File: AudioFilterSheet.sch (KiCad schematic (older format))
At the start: 16 parts, among them P1 R, P2 R, P3 R, P4 R, P5 R, P6 R

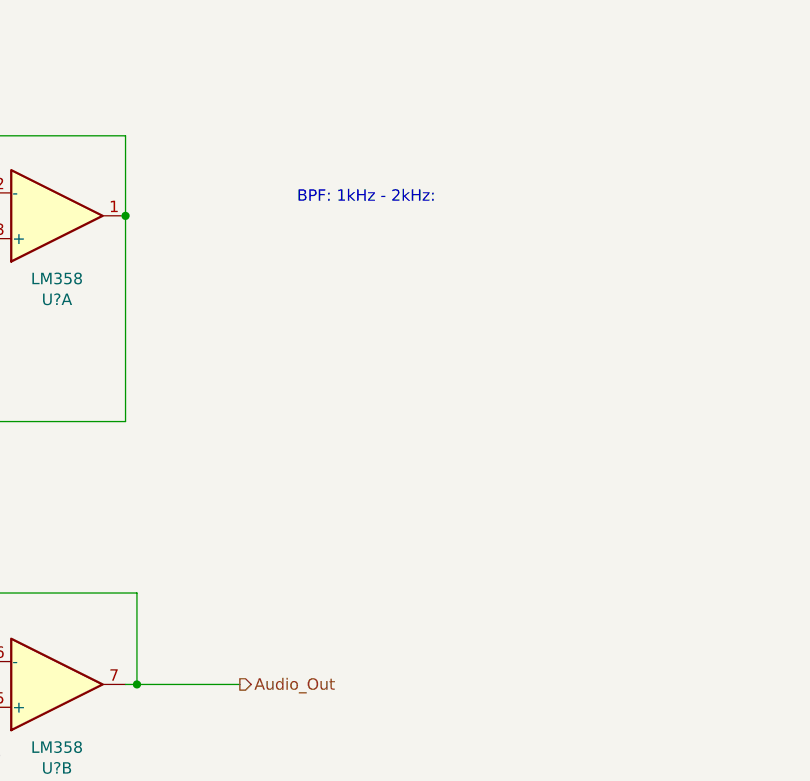
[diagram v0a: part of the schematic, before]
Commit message: Filter calculations, gain stage, oscillation protection
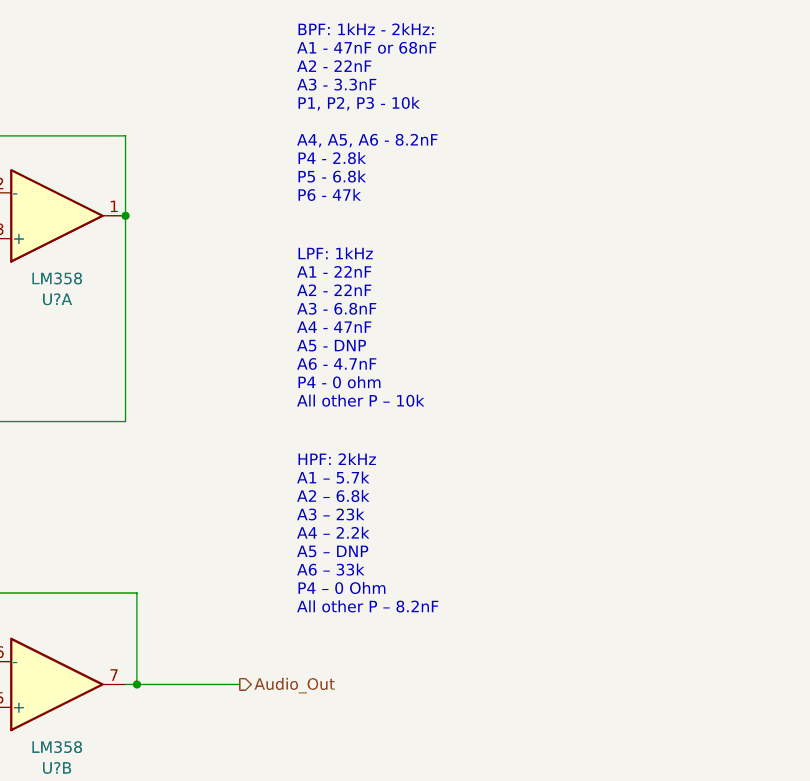
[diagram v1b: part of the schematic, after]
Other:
- note added: "BPF: 1kHz - 2kHz:\nA1 - 47nF or 68nF\nA2 - 22nF\nA3 - 3.3nF\nP1, P2, P3 - 10k\n\nA4, A5, A6 - 8.2nF\nP4 - 2.8k\nP5 - 6.8k\nP6 - 47k"
- note added: "HPF: 2kHz \nA1 – 5.7k \nA2 – 6.8k \nA3 – 23k \nA4 – 2.2k \nA5 – DNP \nA6 – 33k \nP4 – 0 Ohm \nAll other P – 8.2nF"
- note added: "LPF: 1kHz \nA1 - 22nF \nA2 - 22nF \nA3 - 6.8nF \nA4 - 47nF \nA5 - DNP \nA6 - 4.7nF \nP4 - 0 ohm \nAll other P – 10k"
- note removed: "BPF: 1kHz - 2kHz:"
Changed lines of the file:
@@
 	4450 3150 3950 3150
 Text Notes 5800 1450 0    50   ~ 0
-BPF: 1kHz - 2kHz:
+BPF: 1kHz - 2kHz:\nA1 - 47nF or 68nF\nA2 - 22nF\nA3 - 3.3nF\nP1, P2, P3 - 10k\n\nA4, A5, A6 - 8.2nF\nP4 - 2.8k\nP5 - 6.8k\nP6 - 47k
 $Comp
 L Device:C C?
@@
 	8850 2450 8350 2450
 Connection ~ 8350 2450
+Text Notes 5800 2350 0    50   ~ 0
+LPF: 1kHz \nA1 - 22nF \nA2 - 22nF \nA3 - 6.8nF \nA4 - 47nF \nA5 - DNP \nA6 - 4.7nF \nP4 - 0 ohm \nAll other P – 10k
+Text Notes 5800 3250 0    50   ~ 0
+HPF: 2kHz \nA1 – 5.7k \nA2 – 6.8k \nA3 – 23k \nA4 – 2.2k \nA5 – DNP \nA6 – 33k \nP4 – 0 Ohm \nAll other P – 8.2nF
 $EndSCHEMATC

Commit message: WIP
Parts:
- U? (x3): value LM358 -> OPA1678; symbol Amplifier_Operational:LM358 -> Amplifier_Operational:OPA1678
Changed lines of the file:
@@
 $EndComp
 $Comp
-L Amplifier_Operational:LM358 U?
+L Amplifier_Operational:OPA1678 U?
 U 3 1 5E3A2220
 P 8450 2150
@@
 AR Path="/5E41292B/5E39A609/5E3A2220" Ref="U?"  Part="3"
 F 0 "U?" H 8408 2196 50  0000 L CNN
-F 1 "LM358" H 8408 2105 50  0000 L CNN
+F 1 "OPA1678" H 8408 2105 50  0000 L CNN
 F 2 "" H 8450 2150 50  0001 C CNN
 F 3 "http://www.ti.com/lit/ds/symlink/lm2904-n.pdf" H 8450 2150 50  0001 C CNN
@@
 $EndComp
 $Comp
-L Amplifier_Operational:LM358 U?
+L Amplifier_Operational:OPA1678 U?
 U 1 1 5E3A55EC
 P 4750 1500
@@
 AR Path="/5E41292B/5E39A609/5E3A55EC" Ref="U?"  Part="1"
 F 0 "U?" H 4750 1867 50  0000 C CNN
-F 1 "LM358" H 4750 1776 50  0000 C CNN
+F 1 "OPA1678" H 4750 1776 50  0000 C CNN
 F 2 "" H 4750 1500 50  0001 C CNN
 F 3 "http://www.ti.com/lit/ds/symlink/lm2904-n.pdf" H 4750 1500 50  0001 C CNN
@@
 $EndComp
 $Comp
-L Amplifier_Operational:LM358 U?
+L Amplifier_Operational:OPA1678 U?
 U 2 1 5E3A6C1B
 P 4750 3550
@@
 AR Path="/5E41292B/5E39A609/5E3A6C1B" Ref="U?"  Part="2"
 F 0 "U?" H 4750 3917 50  0000 C CNN
-F 1 "LM358" H 4750 3826 50  0000 C CNN
+F 1 "OPA1678" H 4750 3826 50  0000 C CNN
 F 2 "" H 4750 3550 50  0001 C CNN
 F 3 "http://www.ti.com/lit/ds/symlink/lm2904-n.pdf" H 4750 3550 50  0001 C CNN

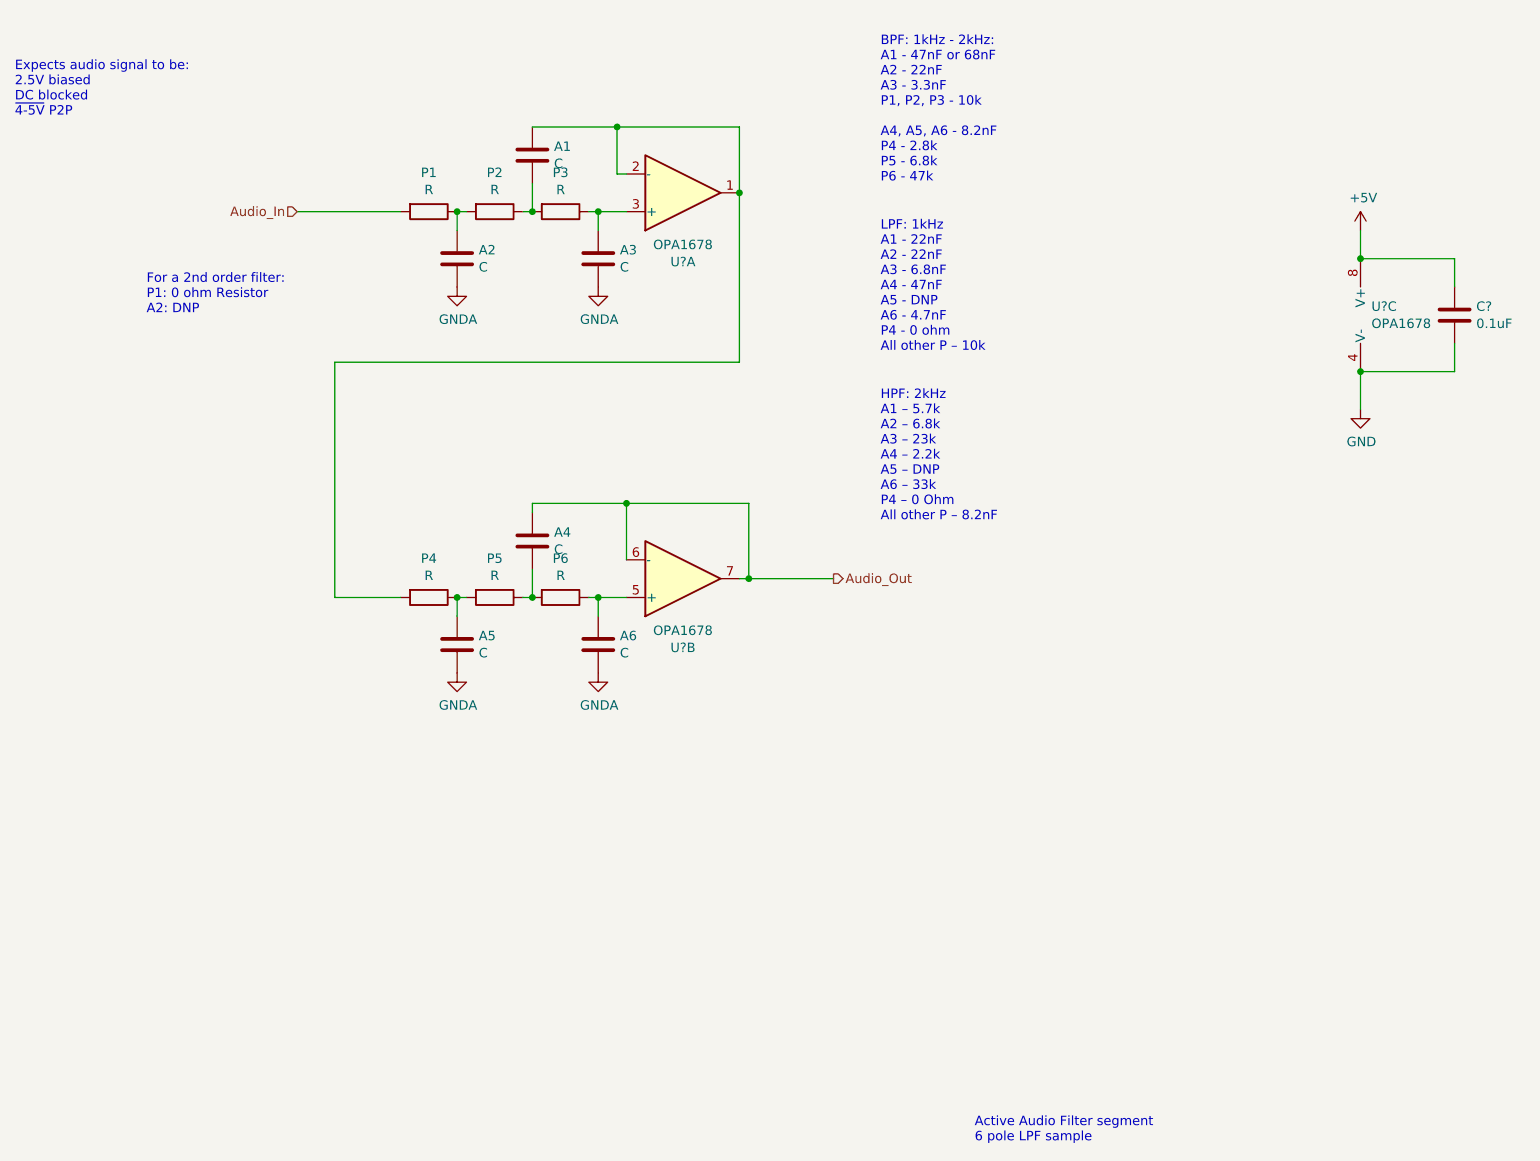
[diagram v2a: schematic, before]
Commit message: Ferrite beads and annotations
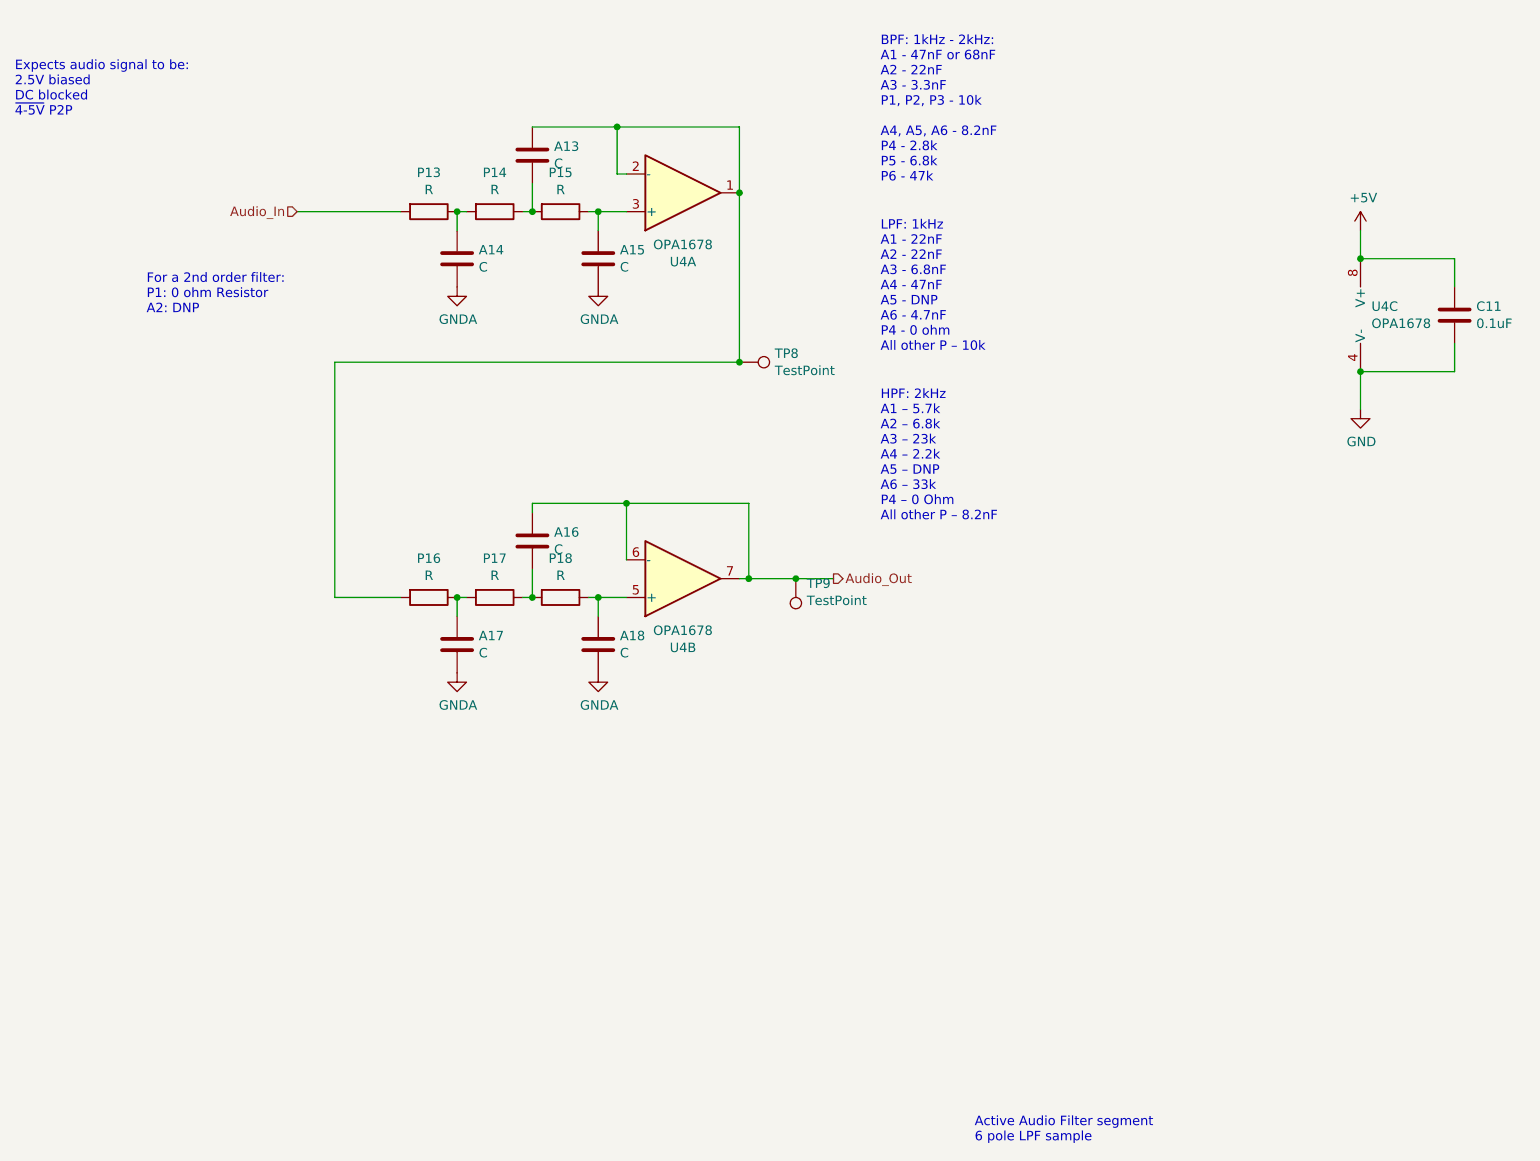
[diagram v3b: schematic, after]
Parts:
- added TP2, TP3: TestPoint, symbol Connector:TestPoint
- gave numbers to parts that had none: 2
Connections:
- net Audio_Out: now also TP3.1
- net at A1.1, P4.2, U1.1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: now also TP2.1

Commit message: Layout, 2020-05 order
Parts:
- removed TP2, TP3: TestPoint, symbol Connector:TestPoint
- A1, A2, A3, A4, A5, A6, C3, P1, P2, P3, P4, P5, P6: footprint (none) -> Capacitors_SMD:C_0805_HandSoldering
- U1: footprint (none) -> SMD_Packages:SOIC-8-N
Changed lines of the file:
@@
 AR Path="/5E41281A/5E39A609/5E39FBC3" Ref="P7"  Part="1"
 AR Path="/5E41292B/5E39A609/5E39FBC3" Ref="P13"  Part="1"
-F 0 "P13" V 3193 1600 50  0000 C CNN
+F 0 "P1" V 3193 1600 50  0000 C CNN
 F 1 "R" V 3284 1600 50  0000 C CNN
-F 2 "" V 3330 1600 50  0001 C CNN
+F 2 "Capacitors_SMD:C_0805_HandSoldering" V 3330 1600 50  0001 C CNN
 F 3 "~" H 3400 1600 50  0001 C CNN
 	1    3400 1600
@@
 AR Path="/5E41281A/5E39A609/5E39FFC0" Ref="P8"  Part="1"
 AR Path="/5E41292B/5E39A609/5E39FFC0" Ref="P14"  Part="1"
-F 0 "P14" V 3543 1600 50  0000 C CNN
+F 0 "P2" V 3543 1600 50  0000 C CNN
 F 1 "R" V 3634 1600 50  0000 C CNN
-F 2 "" V 3680 1600 50  0001 C CNN
+F 2 "Capacitors_SMD:C_0805_HandSoldering" V 3680 1600 50  0001 C CNN
 F 3 "~" H 3750 1600 50  0001 C CNN
 	1    3750 1600
@@
 AR Path="/5E41281A/5E39A609/5E3A018A" Ref="P9"  Part="1"
 AR Path="/5E41292B/5E39A609/5E3A018A" Ref="P15"  Part="1"
-F 0 "P15" V 3893 1600 50  0000 C CNN
+F 0 "P3" V 3893 1600 50  0000 C CNN
 F 1 "R" V 3984 1600 50  0000 C CNN
-F 2 "" V 4030 1600 50  0001 C CNN
+F 2 "Capacitors_SMD:C_0805_HandSoldering" V 4030 1600 50  0001 C CNN
 F 3 "~" H 4100 1600 50  0001 C CNN
 	1    4100 1600
@@
 AR Path="/5E41281A/5E39A609/5E3A0389" Ref="A7"  Part="1"
 AR Path="/5E41292B/5E39A609/5E3A0389" Ref="A13"  Part="1"
-F 0 "A13" H 4065 1346 50  0000 L CNN
+F 0 "A1" H 4065 1346 50  0000 L CNN
 F 1 "C" H 4065 1255 50  0000 L CNN
-F 2 "" H 3988 1150 50  0001 C CNN
+F 2 "Capacitors_SMD:C_0805_HandSoldering" H 3988 1150 50  0001 C CNN
 F 3 "~" H 3950 1300 50  0001 C CNN
 	1    3950 1300
@@
 AR Path="/5E41281A/5E39A609/5E3A041B" Ref="A9"  Part="1"
 AR Path="/5E41292B/5E39A609/5E3A041B" Ref="A15"  Part="1"
-F 0 "A15" H 4415 1896 50  0000 L CNN
+F 0 "A3" H 4415 1896 50  0000 L CNN
 F 1 "C" H 4415 1805 50  0000 L CNN
-F 2 "" H 4338 1700 50  0001 C CNN
+F 2 "Capacitors_SMD:C_0805_HandSoldering" H 4338 1700 50  0001 C CNN
 F 3 "~" H 4300 1850 50  0001 C CNN
 	1    4300 1850
@@
 AR Path="/5E41281A/5E39A609/5E3A0747" Ref="A8"  Part="1"
 AR Path="/5E41292B/5E39A609/5E3A0747" Ref="A14"  Part="1"
-F 0 "A14" H 3665 1896 50  0000 L CNN
+F 0 "A2" H 3665 1896 50  0000 L CNN
 F 1 "C" H 3665 1805 50  0000 L CNN
-F 2 "" H 3588 1700 50  0001 C CNN
+F 2 "Capacitors_SMD:C_0805_HandSoldering" H 3588 1700 50  0001 C CNN
 F 3 "~" H 3550 1850 50  0001 C CNN
 	1    3550 1850
@@
 AR Path="/5E41281A/5E39A609/5E3A1A9D" Ref="#PWR023"  Part="1"
 AR Path="/5E41292B/5E39A609/5E3A1A9D" Ref="#PWR029"  Part="1"
-F 0 "#PWR029" H 3550 1750 50  0001 C CNN
+F 0 "#PWR08" H 3550 1750 50  0001 C CNN
 F 1 "GNDA" H 3555 1827 50  0000 C CNN
 F 2 "" H 3550 2000 50  0001 C CNN
@@
 AR Path="/5E41281A/5E39A609/5E3A1CAA" Ref="#PWR024"  Part="1"
 AR Path="/5E41292B/5E39A609/5E3A1CAA" Ref="#PWR030"  Part="1"
-F 0 "#PWR030" H 4300 1750 50  0001 C CNN
+F 0 "#PWR09" H 4300 1750 50  0001 C CNN
 F 1 "GNDA" H 4305 1827 50  0000 C CNN
 F 2 "" H 4300 2000 50  0001 C CNN
@@
 AR Path="/5E41281A/5E39A609/5E3A2220" Ref="U3"  Part="3"
 AR Path="/5E41292B/5E39A609/5E3A2220" Ref="U4"  Part="3"
-F 0 "U4" H 8408 2196 50  0000 L CNN
+F 0 "U1" H 8408 2196 50  0000 L CNN
 F 1 "OPA1678" H 8408 2105 50  0000 L CNN
-F 2 "" H 8450 2150 50  0001 C CNN
+F 2 "SMD_Packages:SOIC-8-N" H 8450 2150 50  0001 C CNN
 F 3 "http://www.ti.com/lit/ds/symlink/lm2904-n.pdf" H 8450 2150 50  0001 C CNN
 	3    8450 2150
@@
 AR Path="/5E41281A/5E39A609/5E3A55EC" Ref="U3"  Part="1"
 AR Path="/5E41292B/5E39A609/5E3A55EC" Ref="U4"  Part="1"
-F 0 "U4" H 4750 1867 50  0000 C CNN
+F 0 "U1" H 4750 1867 50  0000 C CNN
 F 1 "OPA1678" H 4750 1776 50  0000 C CNN
-F 2 "" H 4750 1500 50  0001 C CNN
+F 2 "SMD_Packages:SOIC-8-N" H 4750 1500 50  0001 C CNN
 F 3 "http://www.ti.com/lit/ds/symlink/lm2904-n.pdf" H 4750 1500 50  0001 C CNN
 	1    4750 1500
@@
 AR Path="/5E41281A/5E39A609/5E3A6C1B" Ref="U3"  Part="2"
 AR Path="/5E41292B/5E39A609/5E3A6C1B" Ref="U4"  Part="2"
-F 0 "U4" H 4750 3917 50  0000 C CNN
+F 0 "U1" H 4750 3917 50  0000 C CNN
 F 1 "OPA1678" H 4750 3826 50  0000 C CNN
-F 2 "" H 4750 3550 50  0001 C CNN
+F 2 "SMD_Packages:SOIC-8-N" H 4750 3550 50  0001 C CNN
 F 3 "http://www.ti.com/lit/ds/symlink/lm2904-n.pdf" H 4750 3550 50  0001 C CNN
 	2    4750 3550
@@
 AR Path="/5E41281A/5E39A609/5E42CFC3" Ref="P10"  Part="1"
 AR Path="/5E41292B/5E39A609/5E42CFC3" Ref="P16"  Part="1"
-F 0 "P16" V 3193 3650 50  0000 C CNN
+F 0 "P4" V 3193 3650 50  0000 C CNN
 F 1 "R" V 3284 3650 50  0000 C CNN
-F 2 "" V 3330 3650 50  0001 C CNN
+F 2 "Capacitors_SMD:C_0805_HandSoldering" V 3330 3650 50  0001 C CNN
 F 3 "~" H 3400 3650 50  0001 C CNN
 	1    3400 3650
@@
 AR Path="/5E41281A/5E39A609/5E42CFCD" Ref="P11"  Part="1"
 AR Path="/5E41292B/5E39A609/5E42CFCD" Ref="P17"  Part="1"
-F 0 "P17" V 3543 3650 50  0000 C CNN
+F 0 "P5" V 3543 3650 50  0000 C CNN
 F 1 "R" V 3634 3650 50  0000 C CNN
-F 2 "" V 3680 3650 50  0001 C CNN
+F 2 "Capacitors_SMD:C_0805_HandSoldering" V 3680 3650 50  0001 C CNN
 F 3 "~" H 3750 3650 50  0001 C CNN
 	1    3750 3650
@@
 AR Path="/5E41281A/5E39A609/5E42CFD7" Ref="P12"  Part="1"
 AR Path="/5E41292B/5E39A609/5E42CFD7" Ref="P18"  Part="1"
-F 0 "P18" V 3893 3650 50  0000 C CNN
+F 0 "P6" V 3893 3650 50  0000 C CNN
 F 1 "R" V 3984 3650 50  0000 C CNN
-F 2 "" V 4030 3650 50  0001 C CNN
+F 2 "Capacitors_SMD:C_0805_HandSoldering" V 4030 3650 50  0001 C CNN
 F 3 "~" H 4100 3650 50  0001 C CNN
 	1    4100 3650
@@
 AR Path="/5E41281A/5E39A609/5E42CFE1" Ref="A10"  Part="1"
 AR Path="/5E41292B/5E39A609/5E42CFE1" Ref="A16"  Part="1"
-F 0 "A16" H 4065 3396 50  0000 L CNN
+F 0 "A4" H 4065 3396 50  0000 L CNN
 F 1 "C" H 4065 3305 50  0000 L CNN
-F 2 "" H 3988 3200 50  0001 C CNN
+F 2 "Capacitors_SMD:C_0805_HandSoldering" H 3988 3200 50  0001 C CNN
 F 3 "~" H 3950 3350 50  0001 C CNN
 	1    3950 3350
@@
 AR Path="/5E41281A/5E39A609/5E42CFEB" Ref="A12"  Part="1"
 AR Path="/5E41292B/5E39A609/5E42CFEB" Ref="A18"  Part="1"
-F 0 "A18" H 4415 3946 50  0000 L CNN
+F 0 "A6" H 4415 3946 50  0000 L CNN
 F 1 "C" H 4415 3855 50  0000 L CNN
-F 2 "" H 4338 3750 50  0001 C CNN
+F 2 "Capacitors_SMD:C_0805_HandSoldering" H 4338 3750 50  0001 C CNN
 F 3 "~" H 4300 3900 50  0001 C CNN
 	1    4300 3900
@@
 AR Path="/5E41281A/5E39A609/5E42CFF5" Ref="A11"  Part="1"
 AR Path="/5E41292B/5E39A609/5E42CFF5" Ref="A17"  Part="1"
-F 0 "A17" H 3665 3946 50  0000 L CNN
+F 0 "A5" H 3665 3946 50  0000 L CNN
 F 1 "C" H 3665 3855 50  0000 L CNN
-F 2 "" H 3588 3750 50  0001 C CNN
+F 2 "Capacitors_SMD:C_0805_HandSoldering" H 3588 3750 50  0001 C CNN
 F 3 "~" H 3550 3900 50  0001 C CNN
 	1    3550 3900
@@
 AR Path="/5E41281A/5E39A609/5E42D008" Ref="#PWR026"  Part="1"
 AR Path="/5E41292B/5E39A609/5E42D008" Ref="#PWR032"  Part="1"
-F 0 "#PWR032" H 3550 3800 50  0001 C CNN
+F 0 "#PWR011" H 3550 3800 50  0001 C CNN
 F 1 "GNDA" H 3555 3877 50  0000 C CNN
 F 2 "" H 3550 4050 50  0001 C CNN
@@
 AR Path="/5E41281A/5E39A609/5E42D012" Ref="#PWR027"  Part="1"
 AR Path="/5E41292B/5E39A609/5E42D012" Ref="#PWR033"  Part="1"
-F 0 "#PWR033" H 4300 3800 50  0001 C CNN
+F 0 "#PWR012" H 4300 3800 50  0001 C CNN
 F 1 "GNDA" H 4305 3877 50  0000 C CNN
 F 2 "" H 4300 4050 50  0001 C CNN
@@
 AR Path="/5E41281A/5E39A609/5E445B11" Ref="#PWR022"  Part="1"
 AR Path="/5E41292B/5E39A609/5E445B11" Ref="#PWR028"  Part="1"
-F 0 "#PWR028" H 8350 1550 50  0001 C CNN
+F 0 "#PWR07" H 8350 1550 50  0001 C CNN
 F 1 "+5V" H 8365 1873 50  0000 C CNN
 F 2 "" H 8350 1700 50  0001 C CNN
@@
 AR Path="/5E41281A/5E39A609/5E44640A" Ref="#PWR025"  Part="1"
 AR Path="/5E41292B/5E39A609/5E44640A" Ref="#PWR031"  Part="1"
-F 0 "#PWR031" H 8350 2400 50  0001 C CNN
+F 0 "#PWR010" H 8350 2400 50  0001 C CNN
 F 1 "GND" H 8355 2477 50  0000 C CNN
 F 2 "" H 8350 2650 50  0001 C CNN
@@
 	3950 3150 3950 3200
 Connection ~ 5100 3550
-Wire Wire Line
-	5100 3550 5350 3550
 Wire Wire Line
 	4450 3450 4450 3150
@@
 AR Path="/5E41281A/5E39A609/5E48E352" Ref="C10"  Part="1"
 AR Path="/5E41292B/5E39A609/5E48E352" Ref="C11"  Part="1"
-F 0 "C11" H 8965 2196 50  0000 L CNN
+F 0 "C3" H 8965 2196 50  0000 L CNN
 F 1 "0.1uF" H 8965 2105 50  0000 L CNN
-F 2 "" H 8888 2000 50  0001 C CNN
+F 2 "Capacitors_SMD:C_0805_HandSoldering" H 8888 2000 50  0001 C CNN
 F 3 "~" H 8850 2150 50  0001 C CNN
 	1    8850 2150
@@
 Text Notes 5800 3250 0    50   ~ 0
 HPF: 2kHz \nA1 – 5.7k \nA2 – 6.8k \nA3 – 23k \nA4 – 2.2k \nA5 – DNP \nA6 – 33k \nP4 – 0 Ohm \nAll other P – 8.2nF
-$Comp
-L Connector:TestPoint TP2
-U 1 1 5EC14518
-P 5050 2400
-AR Path="/5E39A5DA/5E39A609/5EC14518" Ref="TP2"  Part="1"
-AR Path="/5E41281A/5E39A609/5EC14518" Ref="TP6"  Part="1"
-AR Path="/5E41292B/5E39A609/5EC14518" Ref="TP8"  Part="1"
-F 0 "TP8" V 5004 2588 50  0000 L CNN
-F 1 "TestPoint" V 5095 2588 50  0000 L CNN
-F 2 "" H 5250 2400 50  0001 C CNN
-F 3 "~" H 5250 2400 50  0001 C CNN
-	1    5050 2400
-	0    1    1    0
-$EndComp
-Connection ~ 5050 2400
-$Comp
-L Connector:TestPoint TP3
-U 1 1 5EC1599F
-P 5350 3550
-AR Path="/5E39A5DA/5E39A609/5EC1599F" Ref="TP3"  Part="1"
-AR Path="/5E41281A/5E39A609/5EC1599F" Ref="TP7"  Part="1"
-AR Path="/5E41292B/5E39A609/5EC1599F" Ref="TP9"  Part="1"
-F 0 "TP9" H 5292 3576 50  0000 R CNN
-F 1 "TestPoint" H 5292 3667 50  0000 R CNN
-F 2 "" H 5550 3550 50  0001 C CNN
-F 3 "~" H 5550 3550 50  0001 C CNN
-	1    5350 3550
-	-1   0    0    1
-$EndComp
-Connection ~ 5350 3550
-Wire Wire Line
-	5350 3550 5550 3550
+Wire Wire Line
+	5100 3550 5550 3550
 $EndSCHEMATC

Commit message: Backup
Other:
- note added: "BPF: 1kHz - 2kHz:\nA1 - 47nF or 68nF\nA2 - 22nF\nA3 - 3.3nF\nP1, P2, P3 - 10k\n\nCORRECTED:\nP4, P5, P6 - 8.2nF\nA4 - 2.8k\nA5 - 6.8k\nA6 - 47k"
- note removed: "BPF: 1kHz - 2kHz:\nA1 - 47nF or 68nF\nA2 - 22nF\nA3 - 3.3nF\nP1, P2, P3 - 10k\n\nA4, A5, A6 - 8.2nF\nP4 - 2.8k\nP5 - 6.8k\nP6 - 47k"
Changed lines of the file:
@@
 	4450 3150 3950 3150
 Text Notes 5800 1450 0    50   ~ 0
-BPF: 1kHz - 2kHz:\nA1 - 47nF or 68nF\nA2 - 22nF\nA3 - 3.3nF\nP1, P2, P3 - 10k\n\nA4, A5, A6 - 8.2nF\nP4 - 2.8k\nP5 - 6.8k\nP6 - 47k
+BPF: 1kHz - 2kHz:\nA1 - 47nF or 68nF\nA2 - 22nF\nA3 - 3.3nF\nP1, P2, P3 - 10k\n\nCORRECTED:\nP4, P5, P6 - 8.2nF\nA4 - 2.8k\nA5 - 6.8k\nA6 - 47k
 $Comp
 L Device:C C3
